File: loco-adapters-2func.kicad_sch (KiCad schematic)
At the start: 0 parts

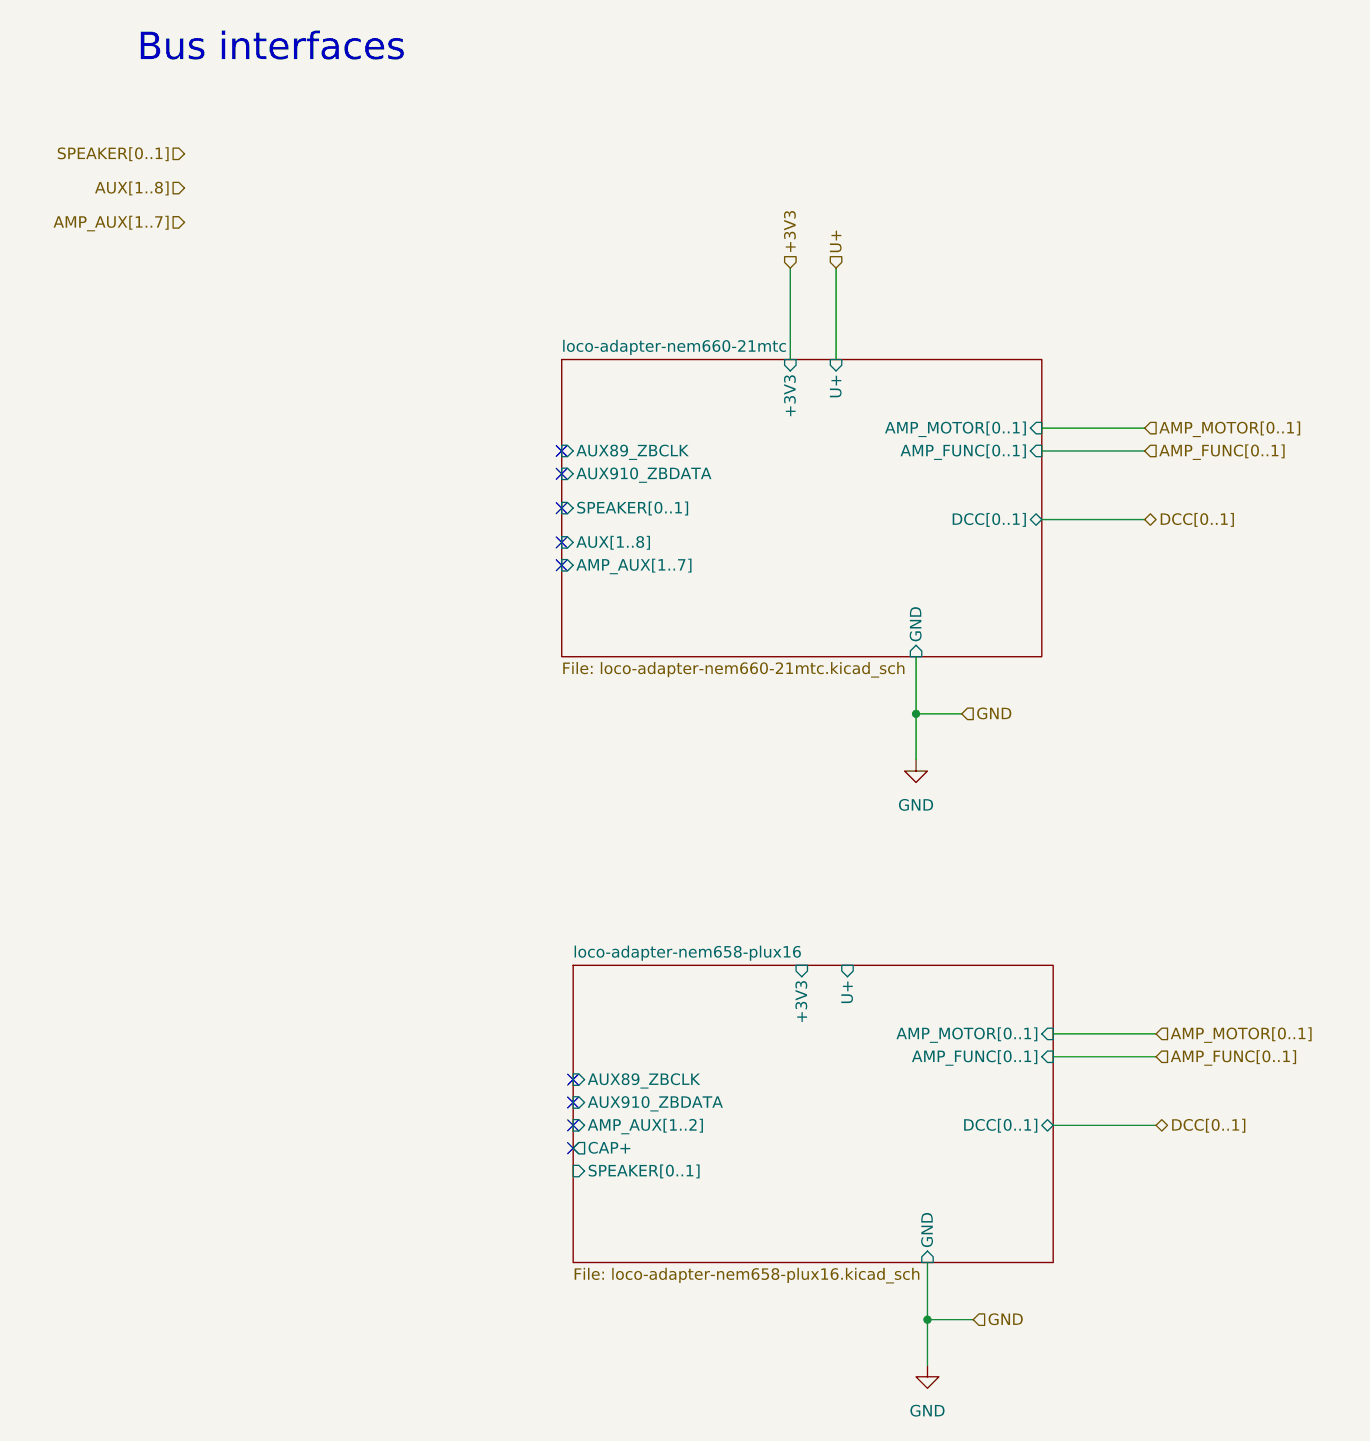
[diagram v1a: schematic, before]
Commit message: Fix - ERC errors
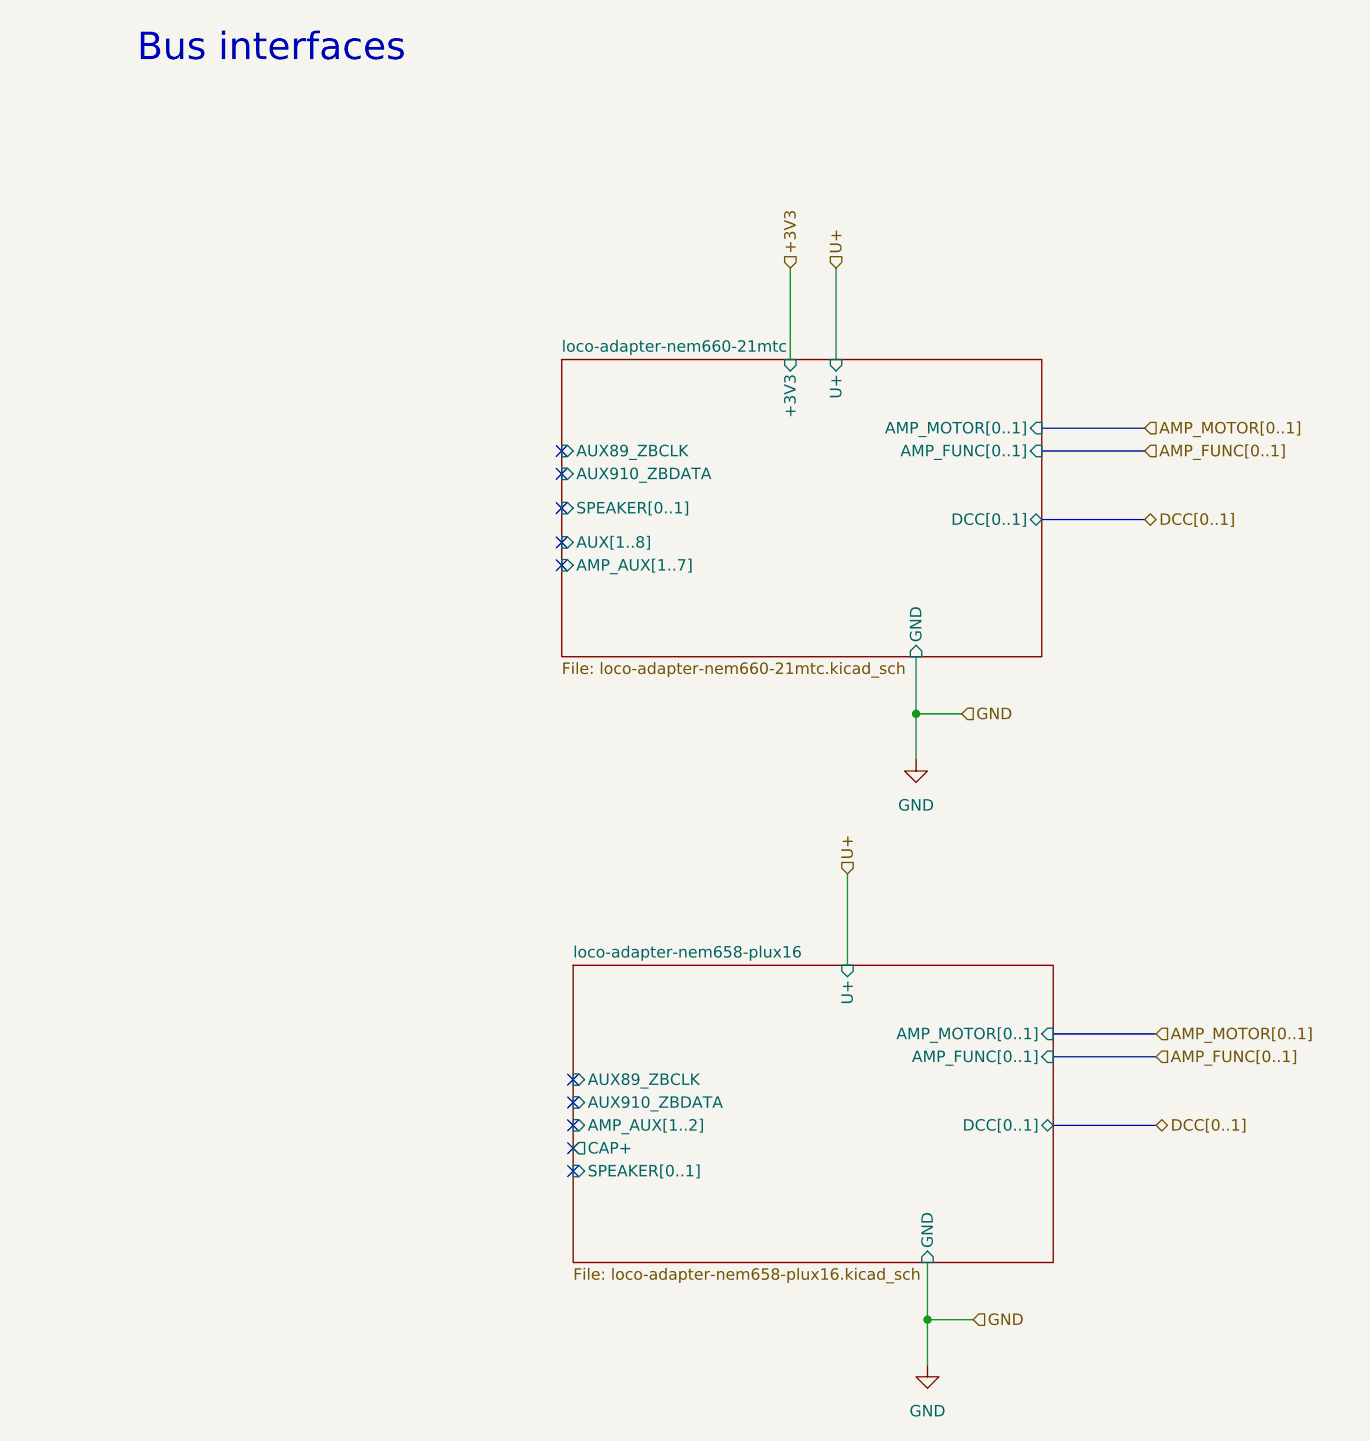
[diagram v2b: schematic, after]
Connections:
- no-connect marks 9 -> 10
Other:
- sheet loco-adapter-nem658-plux16 ports: added none; removed +3V3
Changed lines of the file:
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@@
+	)
+	(no_connect
+		(at 91.44 148.59)
 	)
 	(no_connect
@@
 		)
 	)
-	(wire
-		(pts
-			(xy 156.21 135.89) (xy 144.78 135.89)
+	(bus
+		(pts
+			(xy 144.78 133.35) (xy 156.21 133.35)
+		)
+		(stroke
+			(width 0)
+			(type default)
+		)
+	)
+	(bus
+		(pts
+			(xy 143.51 66.04) (xy 154.94 66.04)
+		)
+		(stroke
+			(width 0)
+			(type default)
+		)
+	)
+	(bus
+		(pts
+			(xy 143.51 76.2) (xy 154.94 76.2)
 		)
 		(stroke
@@
 		)
 	)
-	(wire
-		(pts
-			(xy 154.94 66.04) (xy 143.51 66.04)
+	(bus
+		(pts
+			(xy 144.78 135.89) (xy 156.21 135.89)
 		)
 		(stroke
@@
 	(wire
 		(pts
-			(xy 156.21 143.51) (xy 144.78 143.51)
-		)
-		(stroke
-			(width 0)
-			(type default)
-		)
-	)
-	(wire
-		(pts
-			(xy 154.94 68.58) (xy 143.51 68.58)
+			(xy 121.92 115.57) (xy 121.92 125.73)
 		)
 		(stroke
@@
 		)
 	)
-	(wire
-		(pts
-			(xy 154.94 76.2) (xy 143.51 76.2)
+	(bus
+		(pts
+			(xy 143.51 68.58) (xy 154.94 68.58)
 		)
 		(stroke
@@
 		)
 	)
-	(wire
-		(pts
-			(xy 156.21 133.35) (xy 144.78 133.35)
+	(bus
+		(pts
+			(xy 144.78 143.51) (xy 156.21 143.51)
 		)
 		(stroke
@@
 		)
 	)
+	(hierarchical_label "U+"
+		(shape input)
+		(at 121.92 115.57 90)
+		(effects
+			(font
+				(size 1.27 1.27)
+			)
+			(justify left)
+		)
+	)
 	(hierarchical_label "AMP_MOTOR[0..1]"
 		(shape input)
@@
 		)
 	)
-	(hierarchical_label "SPEAKER[0..1]"
-		(shape input)
-		(at 48.26 35.56 180)
-		(effects
-			(font
-				(size 1.27 1.27)
-			)
-			(justify right)
-		)
-	)
 	(hierarchical_label "AMP_FUNC[0..1]"
 		(shape input)
@@
 			)
 			(justify left)
-		)
-	)
-	(hierarchical_label "AMP_AUX[1..7]"
-		(shape input)
-		(at 48.26 43.18 180)
-		(effects
-			(font
-				(size 1.27 1.27)
-			)
-			(justify right)
 		)
 	)
@@
 			)
 			(justify left)
-		)
-	)
-	(hierarchical_label "AUX[1..8]"
-		(shape input)
-		(at 48.26 39.37 180)
-		(effects
-			(font
-				(size 1.27 1.27)
-			)
-			(justify right)
 		)
 	)
@@
 			)
 		)
-		(pin "+3V3" input
-			(at 116.84 125.73 90)
-			(effects
-				(font
-					(size 1.27 1.27)
-				)
-				(justify right)
-			)
-		)
